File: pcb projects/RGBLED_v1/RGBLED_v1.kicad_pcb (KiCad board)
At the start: 2 copper layers, 7.5 x 2 mm, 16 parts, among them J1 USB_B_Micro, U1 STM32F091RBTx, U2 LP3985IM5-3.3/NOPB

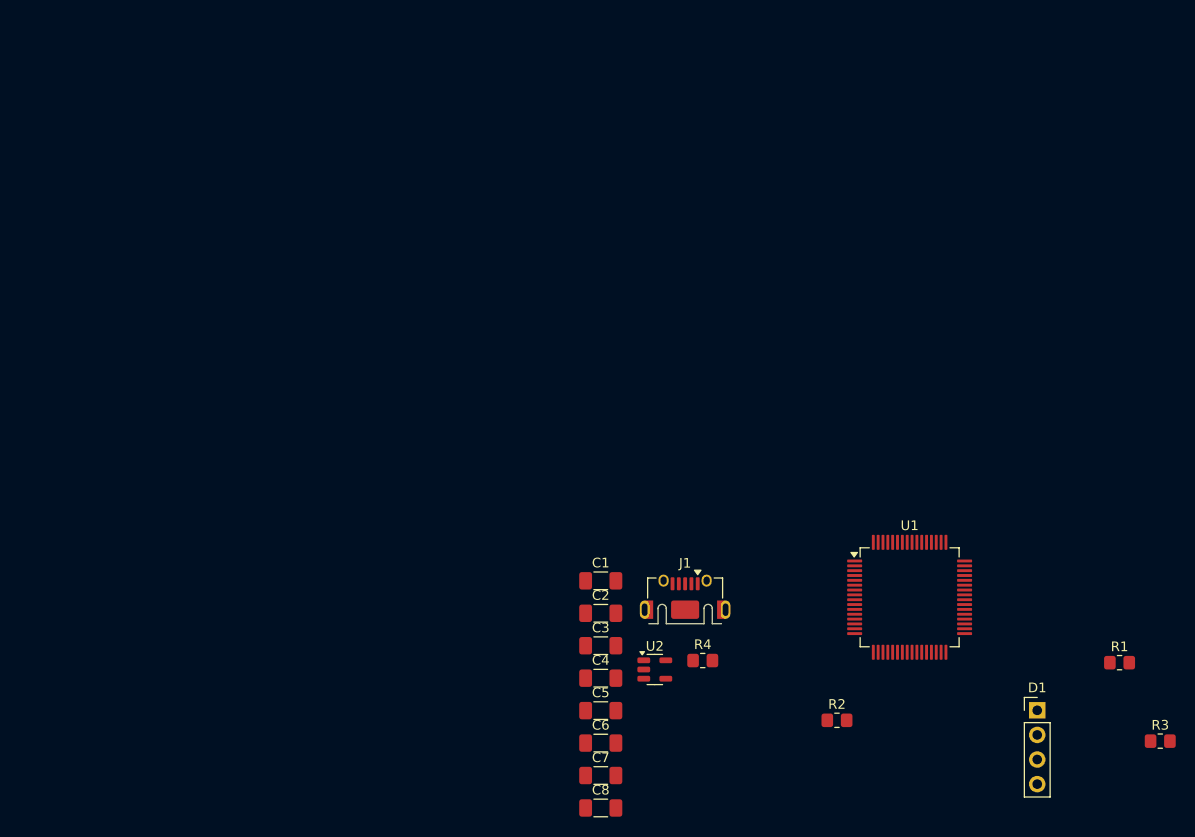
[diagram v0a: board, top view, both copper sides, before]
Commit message: board drawing, footprints except slide switch
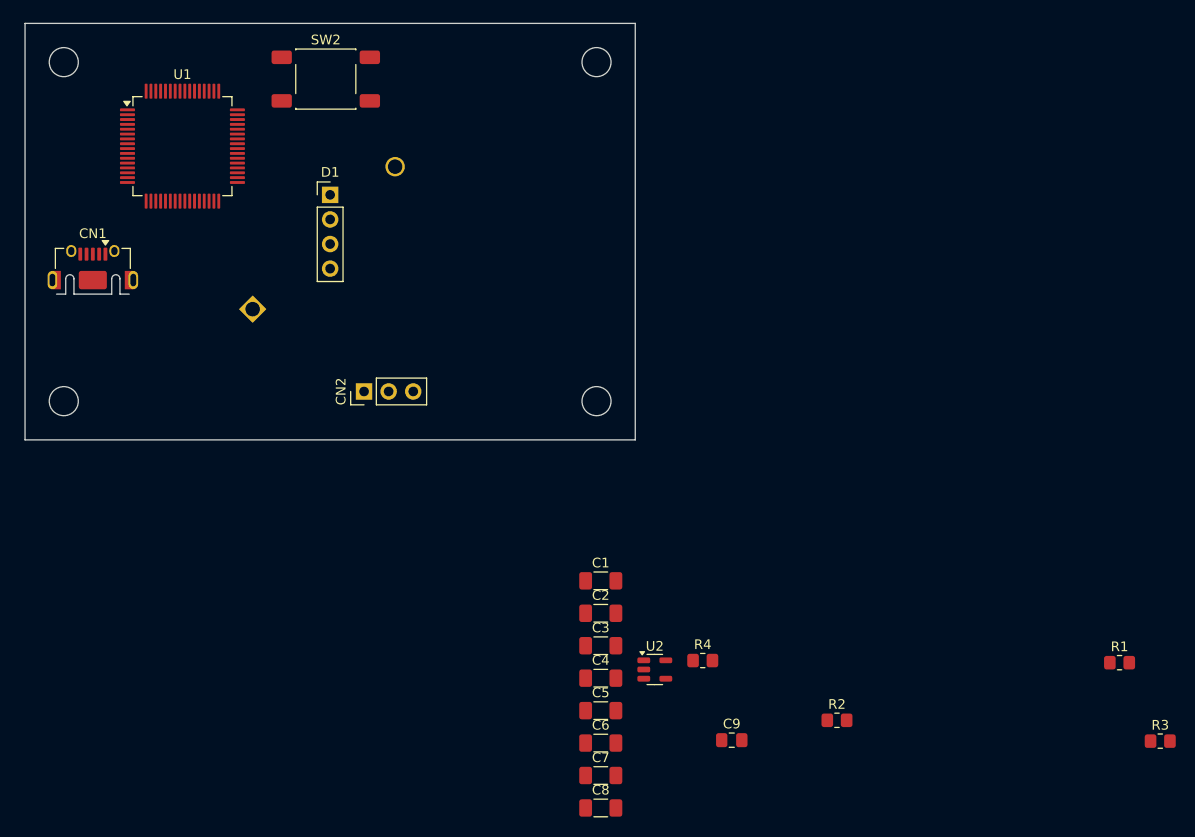
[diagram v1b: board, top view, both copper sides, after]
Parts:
- added BT1: Battery_Cell, Battery:BatteryHolder_MYOUNG_BS-07-A1BJ001_CR2032, B.Cu at (-8.00, 8.00)
- added C9: 22nF, Capacitor_SMD:C_0805_2012Metric_Pad1.18x1.45mm_HandSolder, F.Cu at (41.5, 52.5)
- added CN2: Conn_01x03_Pin, Connector_PinHeader_2.54mm:PinHeader_1x03_P2.54mm_Vertical, F.Cu at (3.50, 16.5)
- added SW2: RESET BUTTON, Button_Switch_SMD:SW_Push_1P1T_NO_E-Switch_TL3301NxxxxxG, F.Cu at (-0.45, -15.8)
- moved D1 90.3 mm to (0.00, -3.80)
- moved U1 88.3 mm to (-15.2, -8.82)
- moved CN1 70.0 mm to (-24.5, 5.35)
- renumbered J1 to CN1
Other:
- board size 7.5 x 2 mm -> 63 x 43 mm

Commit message: mcu finished
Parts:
- added C10: 4.3pF, Capacitor_SMD:C_1206_3216Metric_Pad1.33x1.80mm_HandSolder, F.Cu at (51.1, -7.40)
- added C11: 4.3pF, Capacitor_SMD:C_1206_3216Metric_Pad1.33x1.80mm_HandSolder, F.Cu at (51.1, -4.05)
- added C12: 100nF, Capacitor_SMD:C_1206_3216Metric_Pad1.33x1.80mm_HandSolder, F.Cu at (51.1, -0.70)
- added J1: Conn_02x02_Odd_Even, Connector_PinHeader_2.54mm:PinHeader_2x02_P2.54mm_Vertical, F.Cu at (67.7, 2.73)
- added JP1: SolderJumper, Jumper:SolderJumper-2_P1.3mm_Open_TrianglePad1.0x1.5mm, F.Cu at (56.3, -7.30)
- added L1: Ferrite, Inductor_SMD:L_0603_1608Metric_Pad1.05x0.95mm_HandSolder, F.Cu at (65.1, -4.00)
- added SW1: SW_MEC_5E, Button_Switch_SMD:SW_MEC_5GSH9, F.Cu at (42.3, -0.75)
- added Y1: 32.768kHz, Crystal:Crystal_SMD_HC49-SD_HandSoldering, F.Cu at (47.2, -12.4)
- C4, C5, C6, C7, C8: value 0.01uF -> 100nF
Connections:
- C7 pad 1: GND -> GNDA
- C7 pad 2: +3.3V -> AVDD
- CN2 pad 1: /TCK -> +3.3V
- CN2 pad 2: /TMS -> /TCK
- CN2 pad 3: GND -> /TMS
- U1 pad 12: GND -> GNDA
- U1 pad 13: +3.3V -> AVDD
- U1 pad 3: unconnected-(U1-PC14-Pad3) -> Net-(U1-PC14)
- U1 pad 4: unconnected-(U1-PC15-Pad4) -> Net-(U1-PC15)
- U1 pad 48: +3.3V -> unconnected-(U1-VDDIO2-Pad48)

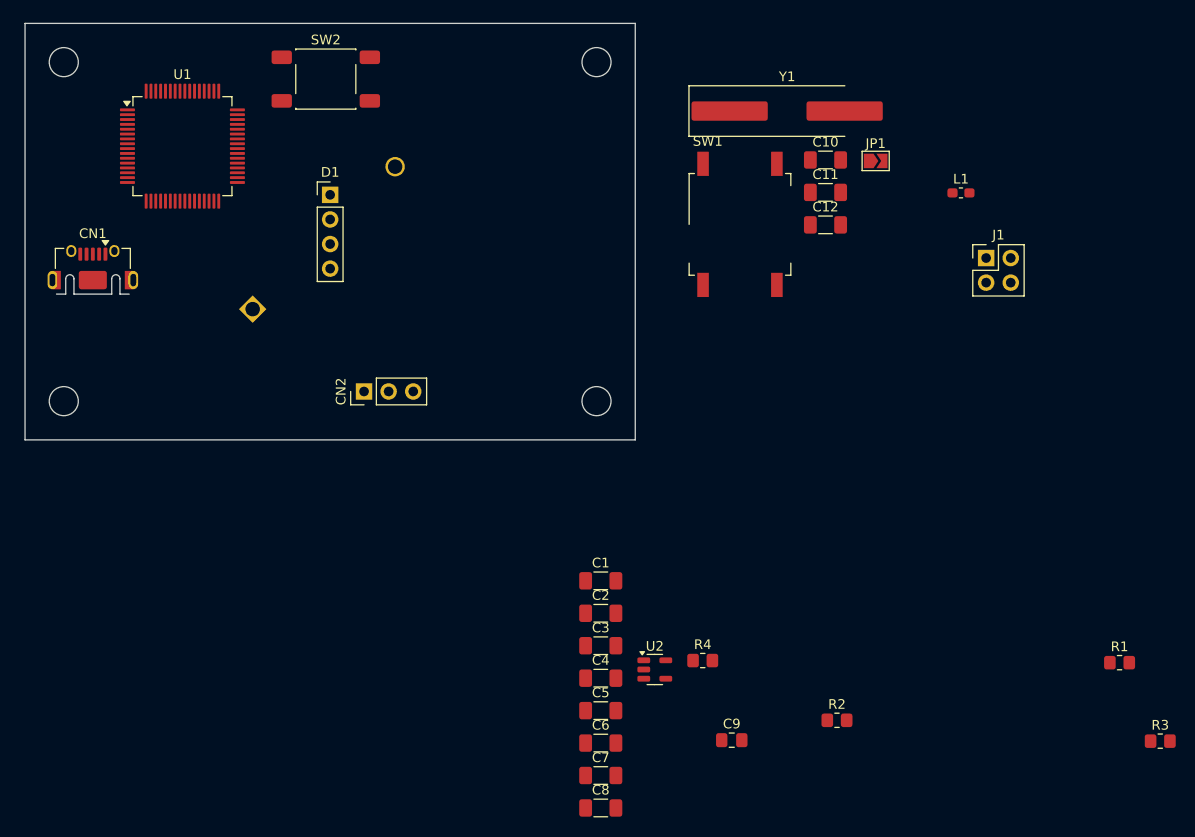
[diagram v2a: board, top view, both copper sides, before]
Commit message: components placement
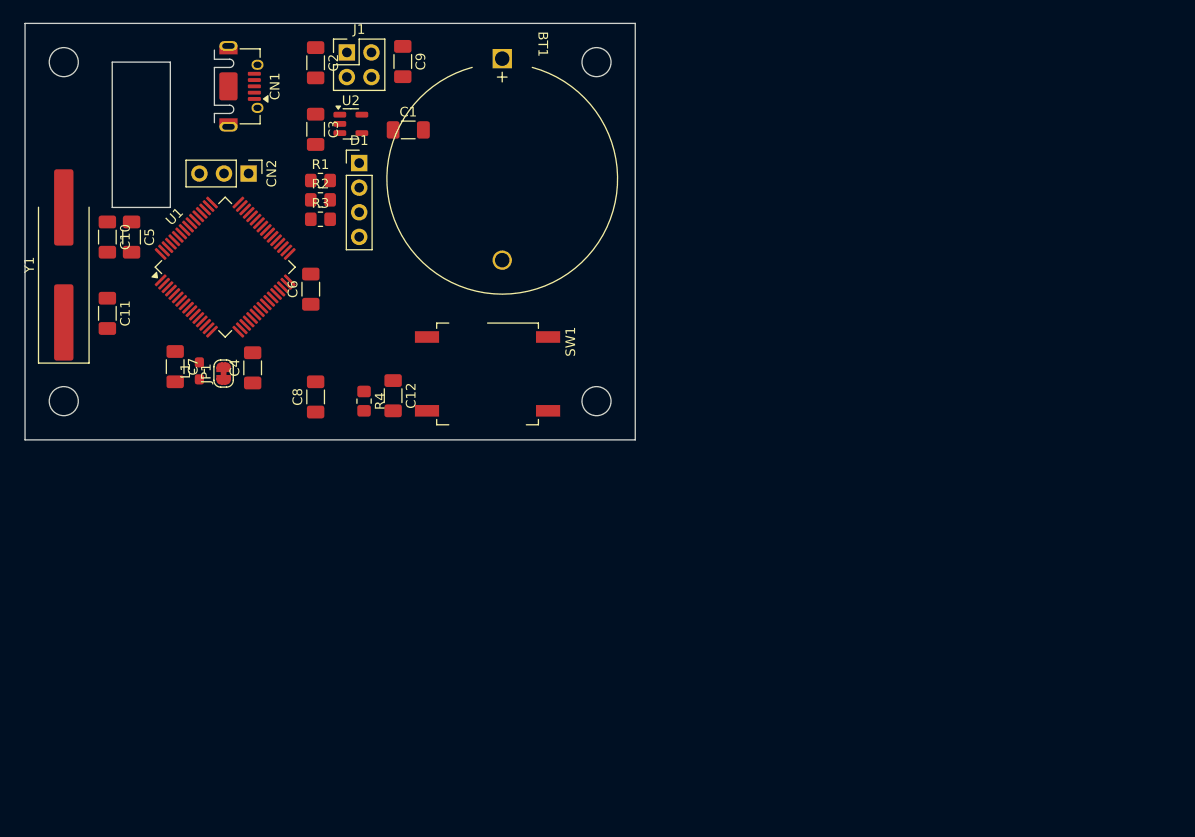
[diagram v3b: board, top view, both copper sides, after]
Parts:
- removed SW2: RESET BUTTON, Button_Switch_SMD:SW_Push_1P1T_NO_E-Switch_TL3301NxxxxxG
- BT1: moved to F.Cu
- C9: footprint Capacitor_SMD:C_0805_2012Metric_Pad1.18x1.45mm_HandSolder -> Capacitor_SMD:C_1206_3216Metric_Pad1.33x1.80mm_HandSolder
- JP1: footprint Jumper:SolderJumper-2_P1.3mm_Open_TrianglePad1.0x1.5mm -> Jumper:SolderJumper-2_P1.3mm_Bridged_RoundedPad1.0x1.5mm
- R1, R3: value 1k -> 150
- R2: value 1k -> 470
- moved R3 102.1 mm to (-1.00, -1.28)
- moved R1 96.4 mm to (-1.00, -5.28)
- moved L1 80.7 mm to (-13.5, 14.4), turned to 90 degrees
- moved C9 77.9 mm to (7.50, -17.6), turned to -90 degrees
- moved Y1 76.4 mm to (-27.5, 3.44), turned to 90 degrees
- moved R2 75.7 mm to (-1.00, -3.28)
- moved C11 75.2 mm to (-23.0, 8.44), turned to -90 degrees
- moved C10 74.6 mm to (-23.0, 0.56), turned to -90 degrees
- moved JP1 70.8 mm to (-11.0, 14.7), turned to 90 degrees
- moved J1 69.3 mm to (1.73, -18.5)
- moved C5 68.8 mm to (-20.5, 0.56), turned to -90 degrees
- moved U2 64.5 mm to (2.14, -11.1)
- moved C2 64.0 mm to (-1.50, -17.4), turned to -90 degrees
- moved C7 60.9 mm to (-16.0, 13.9), turned to -90 degrees
- moved C3 60.9 mm to (-1.50, -10.6), turned to -90 degrees
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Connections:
- J1 pad 2: +3.3V -> Net-(BT1-+)
- J1 pad 3: Net-(BT1-+) -> +3.3V
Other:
- outline, holes or cut-outs redrawn

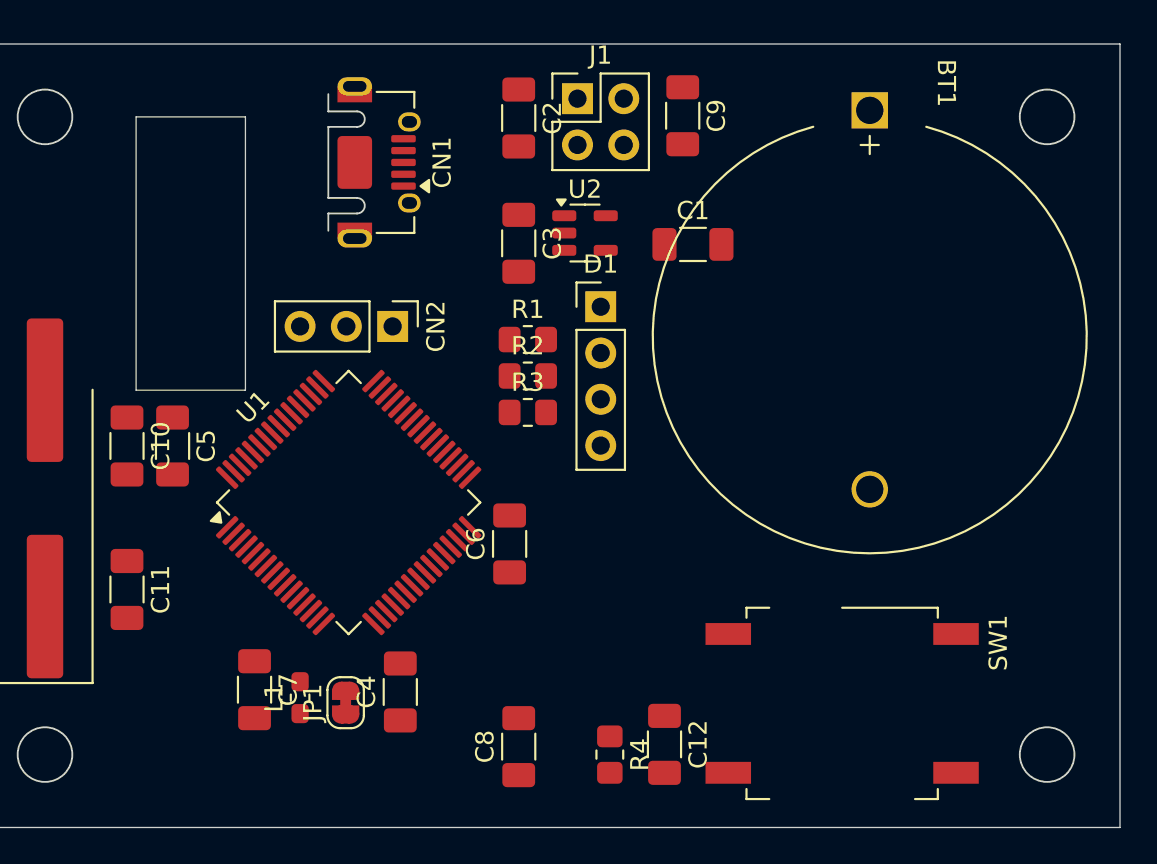
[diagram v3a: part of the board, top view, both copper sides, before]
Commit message: comp changes: stab to tht, cap to tantal; fixed comp placing on pcb
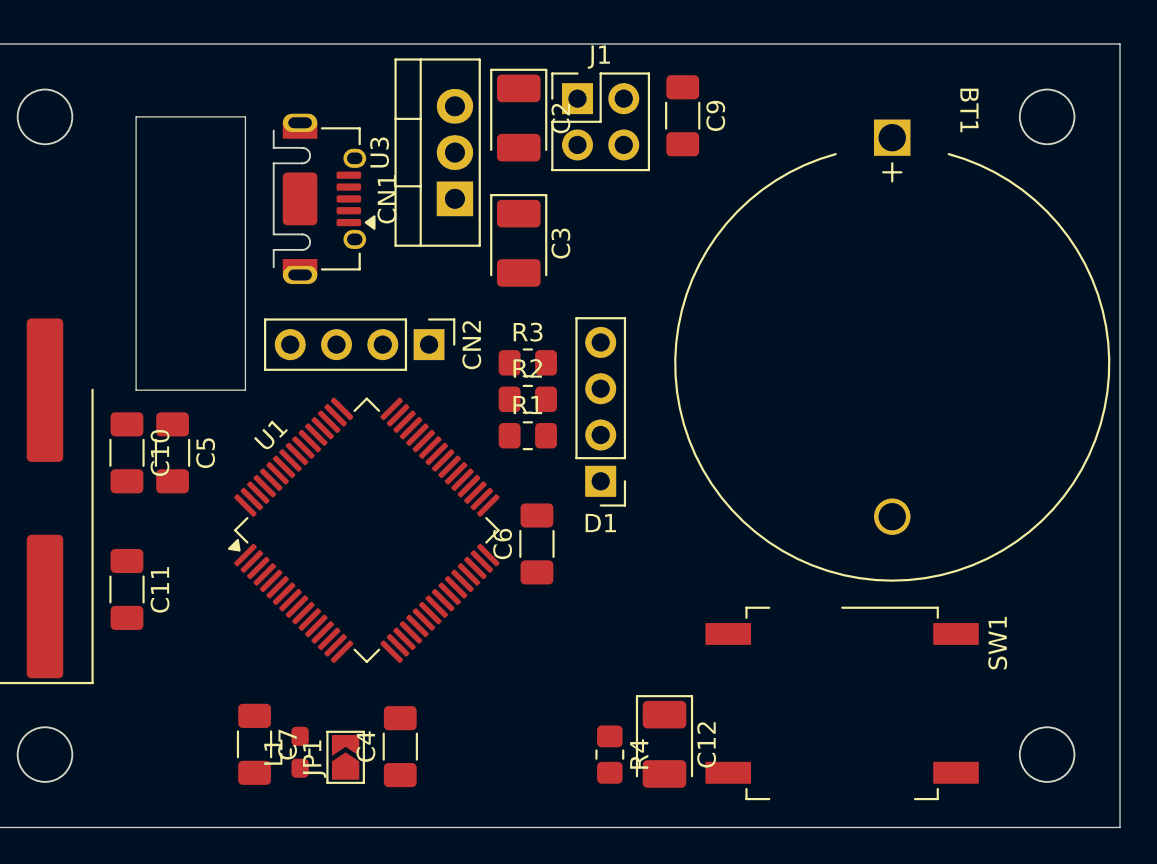
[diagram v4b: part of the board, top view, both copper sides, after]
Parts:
- removed C1: 0.01uF, Capacitor_SMD:C_1206_3216Metric_Pad1.33x1.80mm_HandSolder
- removed C8: 100nF, Capacitor_SMD:C_1206_3216Metric_Pad1.33x1.80mm_HandSolder
- removed U2: LP3985IM5-3.3/NOPB, Package_TO_SOT_SMD:SOT-23-5
- added U3: LM1117T-3.3, Package_TO_SOT_THT:TO-220-3_Vertical, F.Cu at (-5.00, -13.0)
- C12: footprint Capacitor_SMD:C_1206_3216Metric_Pad1.33x1.80mm_HandSolder -> Capacitor_Tantalum_SMD:CP_EIA-3528-21_Kemet-B_HandSolder
- C2: value 1uF -> 100uF; footprint Capacitor_SMD:C_1206_3216Metric_Pad1.33x1.80mm_HandSolder -> Capacitor_Tantalum_SMD:CP_EIA-3528-21_Kemet-B_HandSolder
- C3: value 1uF -> 10uF; footprint Capacitor_SMD:C_1206_3216Metric_Pad1.33x1.80mm_HandSolder -> Capacitor_Tantalum_SMD:CP_EIA-3528-21_Kemet-B_HandSolder
- CN2: footprint Connector_PinHeader_2.54mm:PinHeader_1x03_P2.54mm_Vertical -> Connector_PinHeader_2.54mm:PinHeader_1x04_P2.54mm_Vertical
- JP1: footprint Jumper:SolderJumper-2_P1.3mm_Bridged_RoundedPad1.0x1.5mm -> Jumper:SolderJumper-2_P1.3mm_Open_TrianglePad1.0x1.5mm
- moved D1 9.58 mm to (3.00, 2.50), turned to 180 degrees
- moved R1 5.28 mm to (-1.00, 0.00)
- moved CN1 3.61 mm to (-13.8, -13.0)
- moved C4 3.00 mm to (-8.00, 17.1)
- moved C7 3.00 mm to (-16.0, 16.9)
- moved L1 3.00 mm to (-13.5, 17.4)
- moved JP1 3.00 mm to (-11.0, 17.6)
- moved R3 2.72 mm to (-1.00, -4.00)
- moved CN2 2.24 mm to (-6.42, -5.00)
- moved BT1 1.94 mm to (19.0, -16.4)
- moved U1 1.82 mm to (-9.84, 5.19)
- moved C6 1.50 mm to (-0.50, 5.94)
- moved R2 1.28 mm to (-1.00, -2.00)
- moved C10 0.38 mm to (-23.0, 0.94)
- moved C5 0.38 mm to (-20.5, 0.94)
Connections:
- R1 pad 1: Net-(U1-PA6) -> Net-(U1-PA8)
- R2 pad 1: Net-(U1-PA5) -> Net-(U1-PA9)
- R3 pad 1: Net-(U1-PA7) -> Net-(U1-PA10)
- U1 pad 21: Net-(U1-PA5) -> unconnected-(U1-PA5-Pad21)
- U1 pad 22: Net-(U1-PA6) -> unconnected-(U1-PA6-Pad22)
- U1 pad 23: Net-(U1-PA7) -> unconnected-(U1-PA7-Pad23)
- U1 pad 41: unconnected-(U1-PA8-Pad41) -> Net-(U1-PA8)
- U1 pad 42: unconnected-(U1-PA9-Pad42) -> Net-(U1-PA9)
- U1 pad 43: unconnected-(U1-PA10-Pad43) -> Net-(U1-PA10)
